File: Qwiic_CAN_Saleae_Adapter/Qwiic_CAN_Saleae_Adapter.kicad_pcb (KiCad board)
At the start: 4 copper layers, 20 x 12 mm, 13 parts, among them J1 Screw_Terminal_01x03, J3 Saleae, J4 Conn_QWIIC_Horizontal, U1 MAX33040

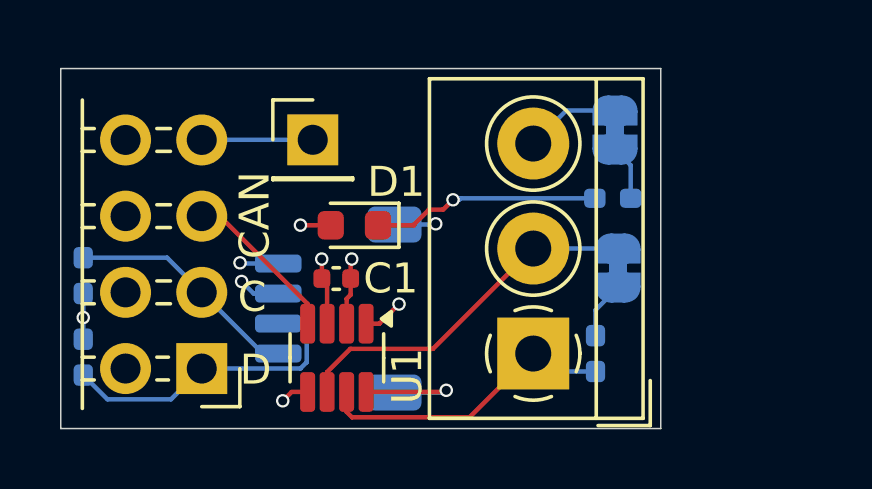
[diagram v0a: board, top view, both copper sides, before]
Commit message: V2 QWIIC board
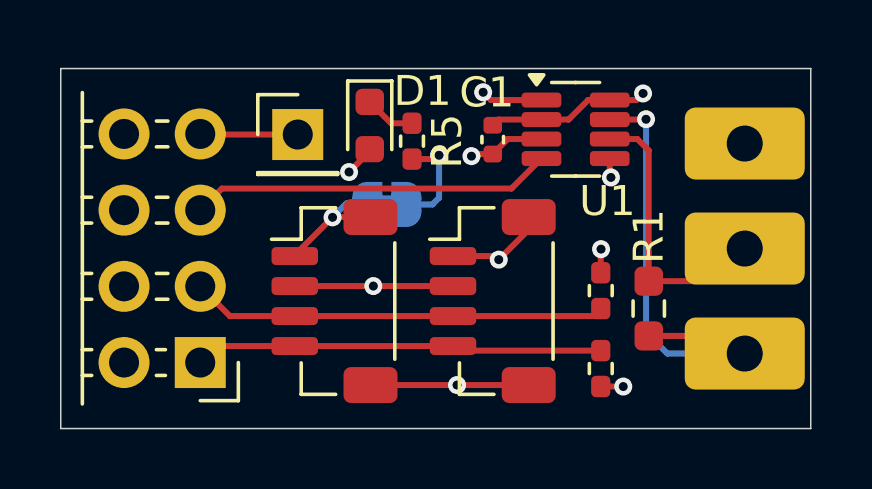
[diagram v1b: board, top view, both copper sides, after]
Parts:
- removed JP1: Jumper_2_Small_Bridged, Jumper:SolderJumper-2_P1.3mm_Bridged_RoundedPad1.0x1.5mm
- added J2: Conn_QWIIC_Vertical, Connector_JST:JST_SH_BM04B-SRSS-TB_1x04-1MP_P1.00mm_Vertical, F.Cu at (64.4, 57.8)
- J1: footprint TerminalBlock_4Ucon:TerminalBlock_4Ucon_1x03_P3.50mm_Horizontal -> SKEC_Footprints:Screw_Terminal_01x03_BoardEdge_Horizontal; moved to B.Cu
- J4: value Conn_QWIIC_Horizontal -> Conn_QWIIC_Vertical; footprint Connector_JST:JST_SH_SM04B-SRSS-TB_1x04-1MP_P1.00mm_Horizontal -> Connector_JST:JST_SH_BM04B-SRSS-TB_1x04-1MP_P1.00mm_Vertical; moved to F.Cu
- R1: footprint Resistor_SMD:R_0402_1005Metric_Pad0.72x0.64mm_HandSolder -> Resistor_SMD:R_0603_1608Metric_Pad0.98x0.95mm_HandSolder; moved to F.Cu
- R2, R3, R5: moved to F.Cu
- moved R3 17.5 mm to (68.0, 60.0)
- moved R2 17.4 mm to (68.0, 57.4)
- moved U1 11.0 mm to (67.2, 52.0), turned to 0 degrees
- moved JP2 8.00 mm to (60.9, 54.5), turned to 0 degrees
- moved J1 7.87 mm to (72.8, 56.0), turned to 0 degrees
- moved C1 6.98 mm to (64.4, 52.4), turned to 90 degrees
- moved R5 6.96 mm to (61.7, 52.4), turned to -90 degrees
- moved D1 3.36 mm to (60.3, 51.9), turned to -90 degrees
- moved R1 2.32 mm to (69.6, 58.0)
- moved TP1 0.53 mm to (57.9, 52.2)
- moved J4 0.28 mm to (59.1, 57.8)
- moved J3 0.21 mm to (54.6, 59.8)
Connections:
- net Net-(J3-Pin_7) renamed /SALEAE_3
- J3 pad 1: /SDA -> /SCL
- J3 pad 3: /SCL -> /SDA
- R1 pad 2: Net-(JP1-B) -> /CAN_L
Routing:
- net /CAN_RX: track 5.40 -> 12.1 mm
- net Net-(D1-K): track 7.61 -> 1.70 mm, vias 1 -> 0
- net /SCL: track 7.82 -> 13.6 mm
- net GND: track 13.5 -> 19.2 mm
- net /CAN_H: track 10.2 -> 15.3 mm, vias 0 -> 1
- net +3V3: track 7.52 -> 12.6 mm, vias 5 -> 6
- net /SDA: track 10.4 -> 13.9 mm
- net /CAN_L: track 12.1 -> 9.47 mm
- net Net-(JP1-B): track 1.91 -> 0.00 mm
- net Net-(JP2-B): track 1.84 -> 3.55 mm, vias 0 -> 1
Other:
- board size 20 x 12 mm -> 25 x 12 mm
- board text added: "GND"
- board text added: "SALEAE ADPTR"
- board text added: "SCL"
- board text added: "SDA"
- board text added: "SKEC V2"
- board text removed: "C"
- board text removed: "D"
- board text removed: "SALEAE ADPTR V1 SKEC"

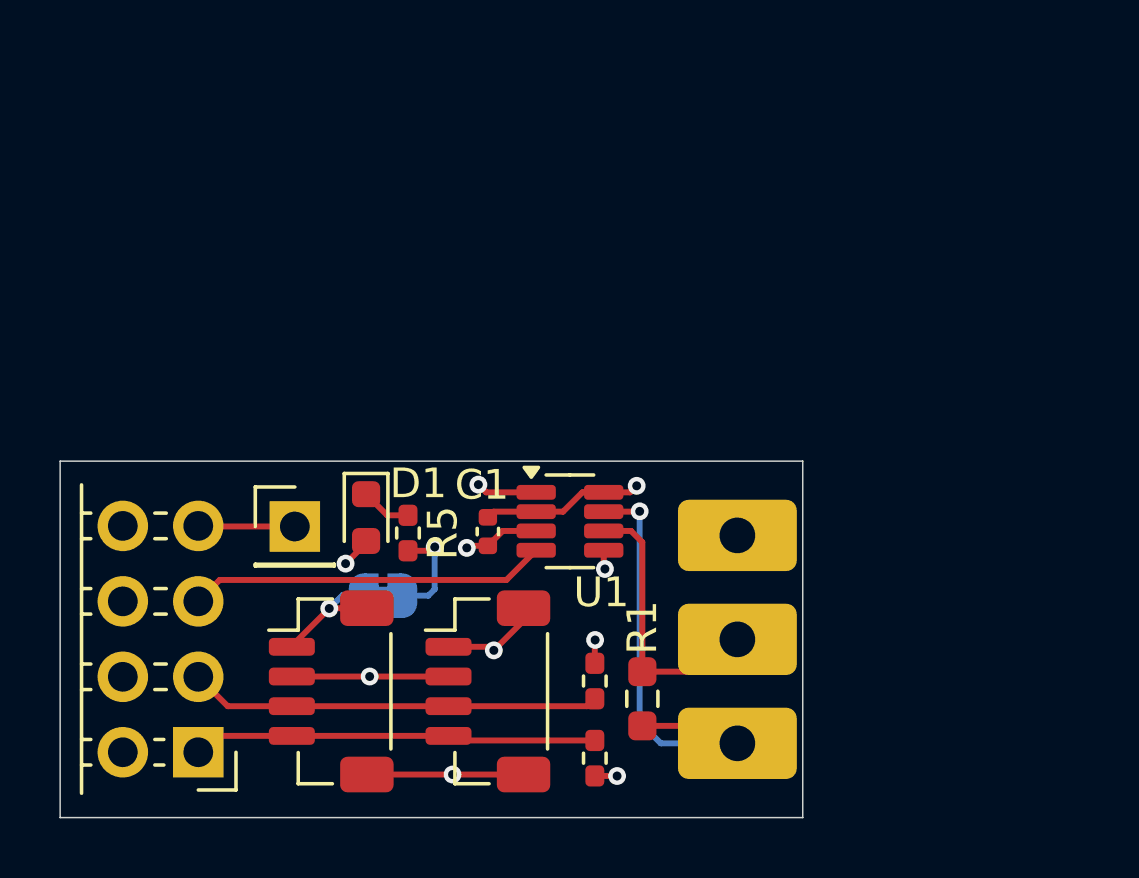
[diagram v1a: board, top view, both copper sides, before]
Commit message: Capture Ideas post v2 and including GDS mount
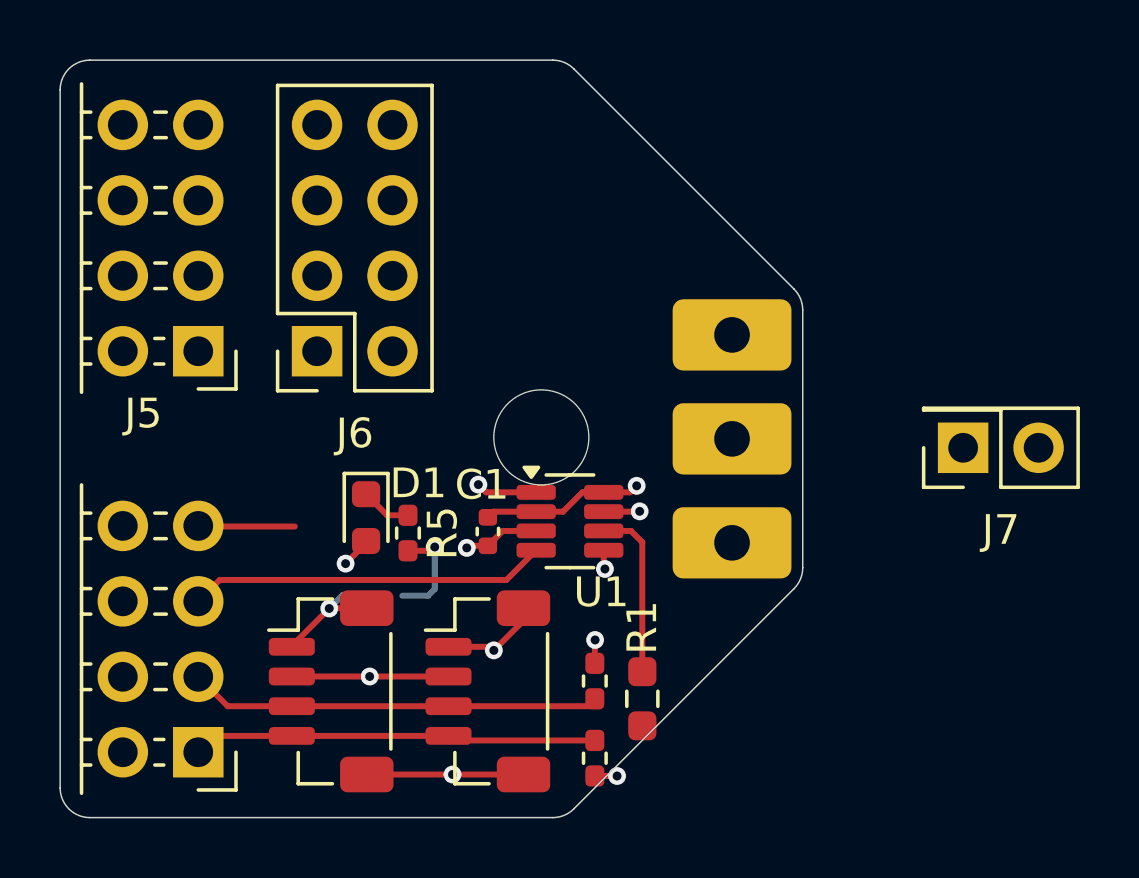
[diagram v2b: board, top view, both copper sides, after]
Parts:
- removed JP2: Jumper_2_Small_Bridged, Jumper:SolderJumper-2_P1.3mm_Bridged_RoundedPad1.0x1.5mm
- removed TP1: TestPoint, Connector_PinHeader_2.54mm:PinHeader_1x01_P2.54mm_Vertical
- added H1: M3, MountingHole:MountingHole_3.2mm_M3_DIN965, F.Cu at (66.2, 49.2)
- added J5: Saleae, Connector_PinHeader_2.54mm:PinHeader_2x04_P2.54mm_Horizontal, F.Cu at (54.6, 46.3)
- added J6: Saleae, Connector_PinSocket_2.54mm:PinSocket_2x04_P2.54mm_Vertical, F.Cu at (58.6, 46.3)
- added J7: Conn_02x01, Connector_PinSocket_2.54mm:PinSocket_2x01_P2.54mm_Vertical, F.Cu at (80.4, 49.5)
- moved J1 6.75 mm to (72.6, 49.2)
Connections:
- R5 pad 2: Net-(JP2-B) -> GND
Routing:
- net /CAN_H: track 15.3 -> 1.21 mm
- net /CAN_L: track 9.47 -> 5.81 mm
- net GND: track 19.2 -> 22.8 mm, vias 5 -> 6
- net Net-(JP2-B): track 3.55 -> 0.00 mm, vias 1 -> 0
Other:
- board size 25 x 12 mm -> 25 x 25.5 mm
- board text added: "SKEC V3"
- board text removed: "SKEC V2"

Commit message: V3 of Saleae Adapter
Added the other 4 channels and a mounting hole for the Gridfinity holder
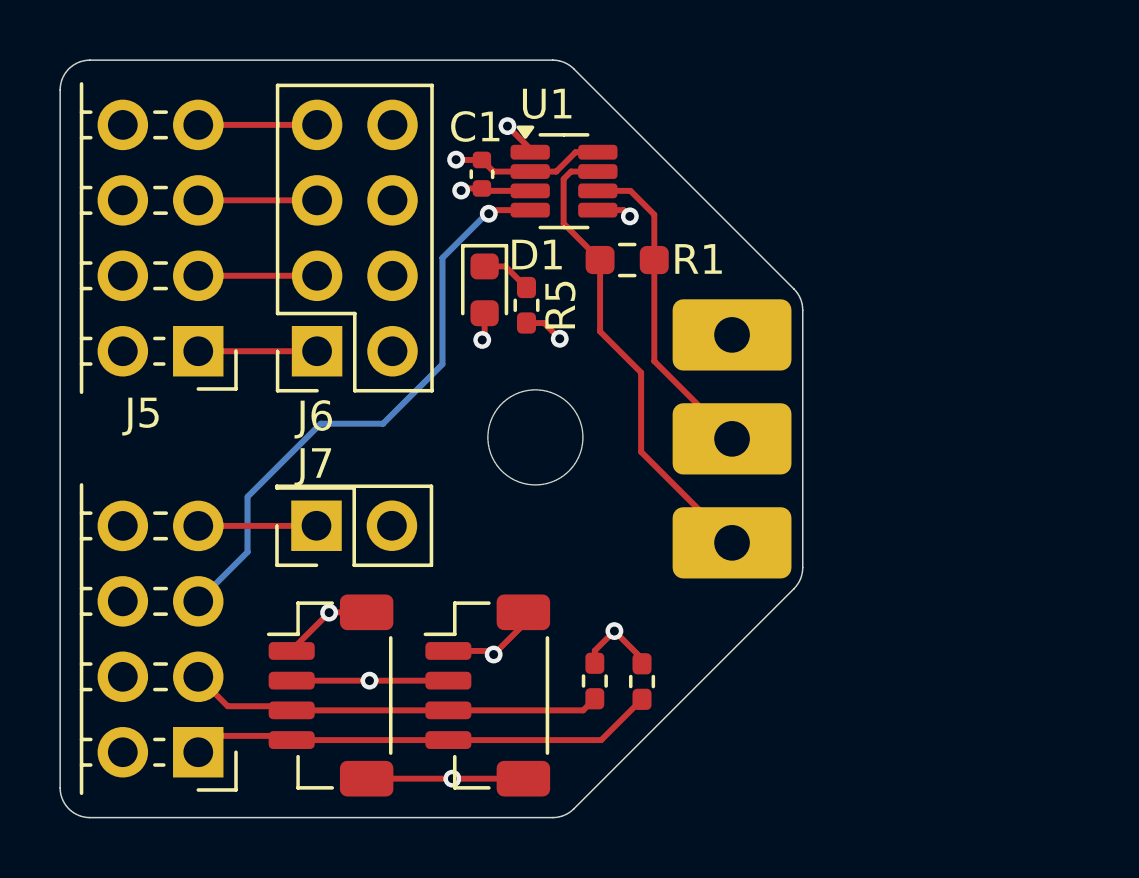
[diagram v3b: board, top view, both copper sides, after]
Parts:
- moved J7 21.9 mm to (58.6, 52.2)
- moved R1 14.8 mm to (69.1, 43.2), turned to 0 degrees
- moved C1 12.0 mm to (64.2, 40.3)
- moved U1 11.5 mm to (67.0, 40.6)
- moved R5 8.64 mm to (65.7, 44.8)
- moved D1 8.64 mm to (64.3, 44.2)
- moved R3 3.03 mm to (69.6, 57.4), turned to -90 degrees
- moved H1 0.20 mm to (66.0, 49.2)
- moved J2 0.14 mm to (64.4, 57.9)
- moved J4 0.14 mm to (59.1, 57.9)
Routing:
- net /CAN_H: track 1.21 -> 15.9 mm, vias 1 -> 0
- net /CAN_RX: track 12.1 -> 19.8 mm, vias 0 -> 1
- net /CAN_L: track 5.81 -> 10.9 mm
- net /SALEAE_7: track 0.00 -> 4.00 mm
- net /SALEAE_6: track 0.00 -> 4.00 mm
- net /SALEAE_5: track 0.00 -> 4.00 mm
- net /SALEAE_4: track 0.00 -> 4.00 mm
- net GND: track 22.8 -> 19.5 mm
- net /SCL: track 13.6 -> 16.0 mm
- net /SALEAE_3: track 3.26 -> 4.01 mm
- net +3V3: track 12.6 -> 12.7 mm, vias 6 -> 5
